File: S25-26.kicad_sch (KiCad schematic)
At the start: 17 parts, among them IC1 CMV4000-3E5M0PN

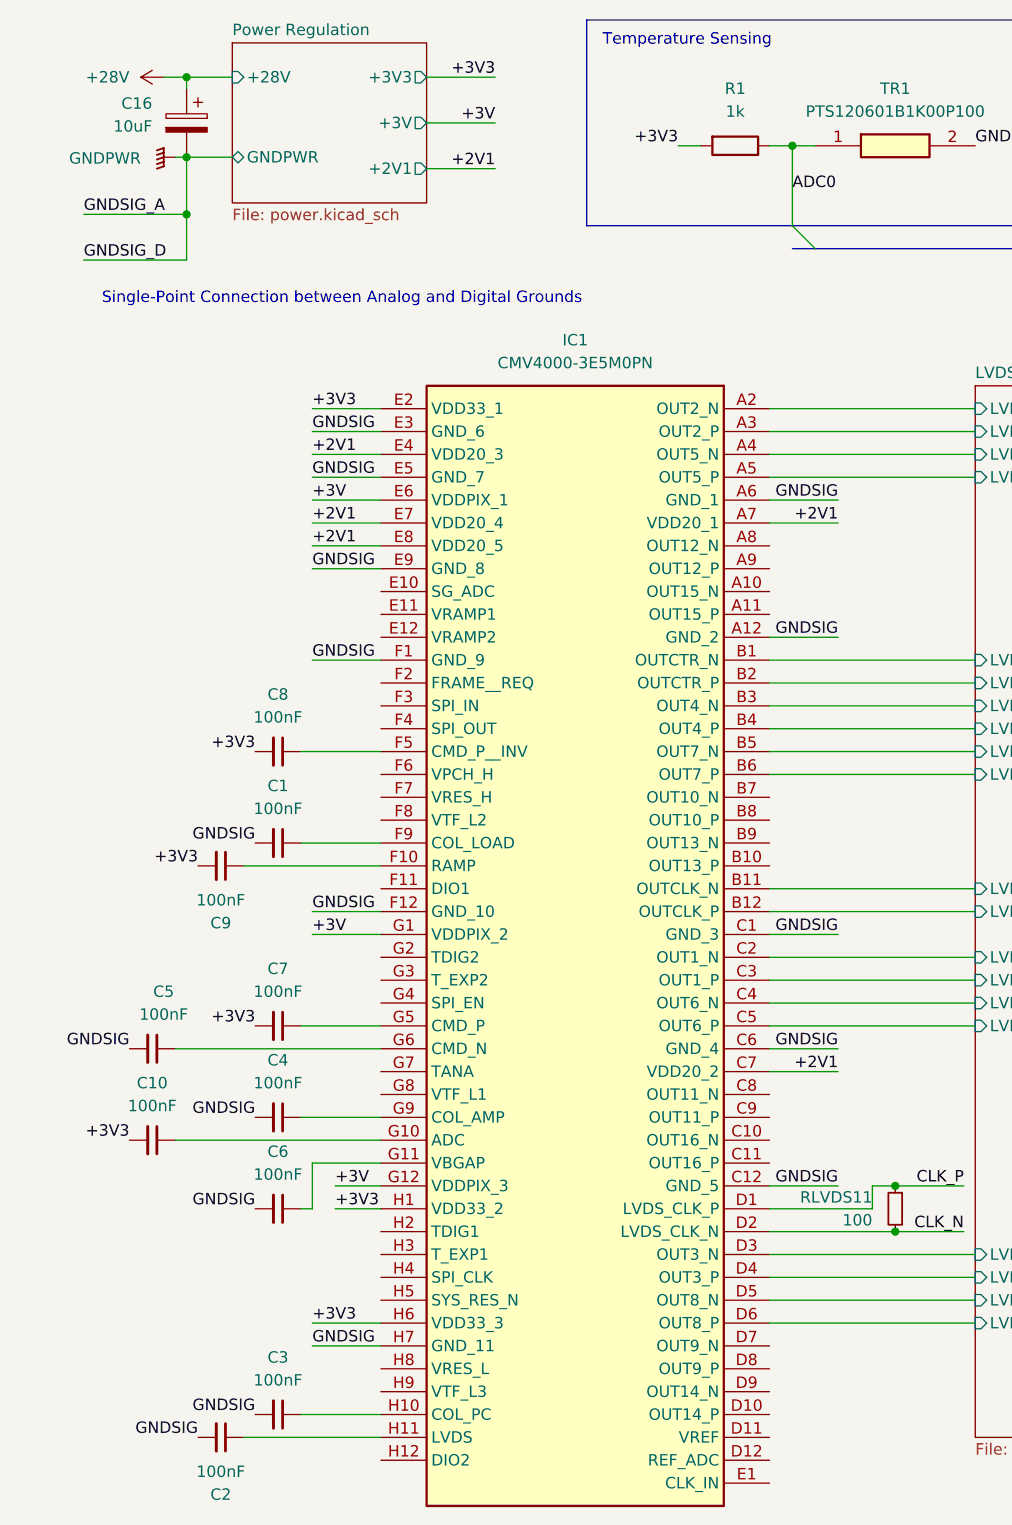
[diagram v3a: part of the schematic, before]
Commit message: Some Colors; GND net ties
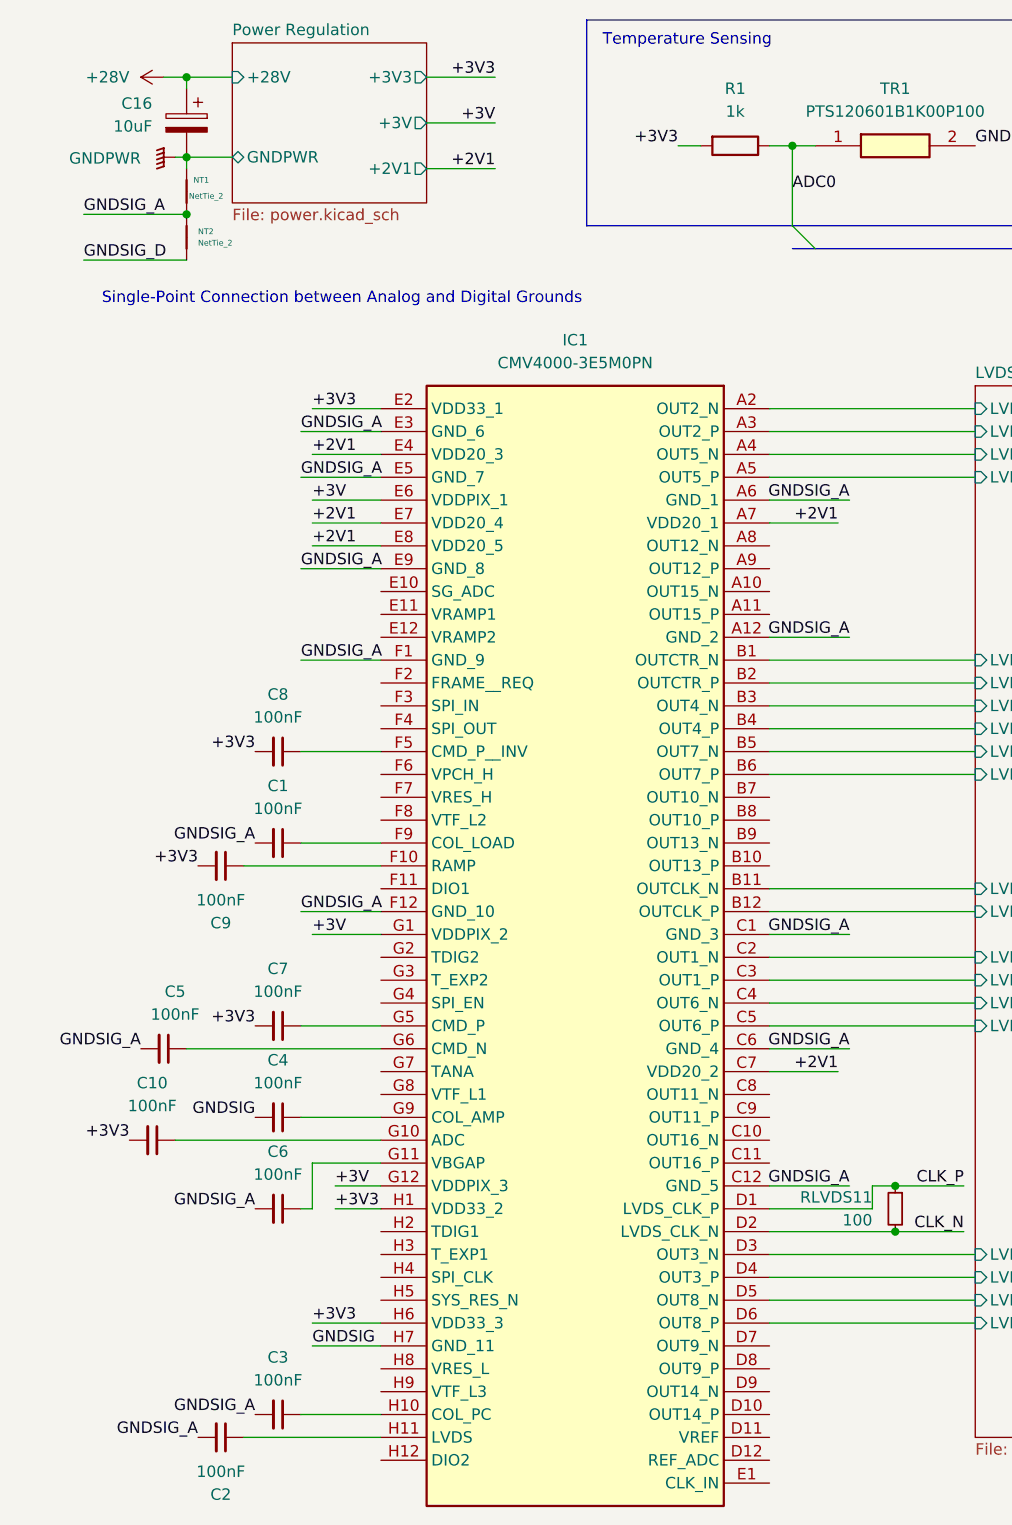
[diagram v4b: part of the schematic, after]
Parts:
- added NT1, NT2: NetTie_2, symbol Device:NetTie_2
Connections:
- net GNDPWR: now also NT1.2
- net GNDSIG: no longer C1.2, C2.2, C3.2, C5.2, C6.2, IC1.A12 (GND_2), IC1.A6 (GND_1), IC1.C1 (GND_3), IC1.C12 (GND_5), IC1.C6 (GND_4), IC1.E3 (GND_6), IC1.E5 (GND_7), IC1.E9 (GND_8), IC1.F1 (GND_9), IC1.F12 (GND_10)
- new net GNDSIG_A: C1.2, C2.2, C3.2, C5.2, C6.2, IC1.A12 (GND_2), IC1.A6 (GND_1), IC1.C1 (GND_3), IC1.C12 (GND_5), IC1.C6 (GND_4), IC1.E3 (GND_6), IC1.E5 (GND_7), IC1.E9 (GND_8), IC1.F1 (GND_9), IC1.F12 (GND_10), NT1.1, NT2.2
- new net GNDSIG_D: NT2.1
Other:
- moved on the sheet: C5
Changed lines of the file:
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@@
 	(wire
 		(pts
-			(xy 40.64 85.09) (xy 48.26 85.09)
+			(xy 39.37 85.09) (xy 48.26 85.09)
 		)
 		(stroke
@@
 	(wire
 		(pts
-			(xy 26.67 29.21) (xy 26.67 35.56)
-		)
-		(stroke
-			(width 0)
-			(type default)
-		)
-	)
-	(wire
-		(pts
-			(xy 99.06 128.27) (xy 91.44 128.27)
+			(xy 100.33 128.27) (xy 91.44 128.27)
 		)
 		(stroke
@@
 	(wire
 		(pts
-			(xy 26.67 35.56) (xy 26.67 40.64)
-		)
-		(stroke
-			(width 0)
-			(type default)
-		)
-	)
-	(wire
-		(pts
 			(xy 171.45 57.15) (xy 177.8 57.15)
 		)
@@
 	(wire
 		(pts
-			(xy 91.44 143.51) (xy 99.06 143.51)
+			(xy 91.44 143.51) (xy 100.33 143.51)
 		)
 		(stroke
@@
 	(wire
 		(pts
-			(xy 40.64 113.03) (xy 48.26 113.03)
+			(xy 39.37 113.03) (xy 48.26 113.03)
 		)
 		(stroke
@@
 	(wire
 		(pts
+			(xy 26.67 29.21) (xy 26.67 30.48)
+		)
+		(stroke
+			(width 0)
+			(type default)
+		)
+	)
+	(wire
+		(pts
 			(xy 40.64 72.39) (xy 48.26 72.39)
 		)
@@
 	(wire
 		(pts
-			(xy 99.06 82.55) (xy 91.44 82.55)
+			(xy 100.33 82.55) (xy 91.44 82.55)
 		)
 		(stroke
@@
 	(wire
 		(pts
-			(xy 40.64 64.77) (xy 48.26 64.77)
+			(xy 39.37 64.77) (xy 48.26 64.77)
 		)
 		(stroke
@@
 	(wire
 		(pts
-			(xy 25.4 128.27) (xy 48.26 128.27)
+			(xy 26.67 128.27) (xy 48.26 128.27)
 		)
 		(stroke
@@
 	(wire
 		(pts
-			(xy 99.06 67.31) (xy 91.44 67.31)
+			(xy 100.33 67.31) (xy 91.44 67.31)
 		)
 		(stroke
@@
 	(wire
 		(pts
-			(xy 40.64 74.93) (xy 48.26 74.93)
+			(xy 39.37 74.93) (xy 48.26 74.93)
 		)
 		(stroke
@@
 	(wire
 		(pts
-			(xy 99.06 115.57) (xy 91.44 115.57)
+			(xy 100.33 115.57) (xy 91.44 115.57)
 		)
 		(stroke
@@
 	(wire
 		(pts
-			(xy 40.64 59.69) (xy 48.26 59.69)
+			(xy 39.37 59.69) (xy 48.26 59.69)
 		)
 		(stroke
@@
 		)
 	)
-	(label "GNDSIG"
-		(at 99.06 115.57 180)
+	(label "GNDSIG_A"
+		(at 100.33 115.57 180)
 		(fields_autoplaced yes)
 		(effects
@@
 		)
 	)
-	(label "GNDSIG"
+	(label "GNDSIG_A"
 		(at 34.29 105.41 180)
 		(fields_autoplaced yes)
@@
 	(label "ADC0"
 		(at 171.45 57.15 0)
+		(fields_autoplaced yes)
 		(effects
 			(font
@@
 		)
 	)
-	(label "GNDSIG"
-		(at 99.06 67.31 180)
+	(label "GNDSIG_A"
+		(at 100.33 67.31 180)
 		(fields_autoplaced yes)
 		(effects
@@
 		)
 	)
-	(label "GNDSIG"
+	(label "GNDSIG_A"
 		(at 34.29 146.05 180)
 		(fields_autoplaced yes)
@@
 		)
 	)
-	(label "GNDSIG"
+	(label "GNDSIG_A"
 		(at 34.29 168.91 180)
 		(fields_autoplaced yes)
@@
 	(label "ADC1"
 		(at 142.24 33.02 0)
+		(fields_autoplaced yes)
 		(effects
 			(font
@@
 		)
 	)
-	(label "GNDSIG"
-		(at 40.64 85.09 0)
+	(label "GNDSIG_A"
+		(at 39.37 85.09 0)
 		(fields_autoplaced yes)
 		(effects
@@
 		)
 	)
-	(label "GNDSIG"
-		(at 40.64 74.93 0)
+	(label "GNDSIG_A"
+		(at 39.37 74.93 0)
 		(fields_autoplaced yes)
 		(effects
@@
 	(label "ADC1"
 		(at 171.45 60.96 0)
+		(fields_autoplaced yes)
 		(effects
 			(font
@@
 		)
 	)
-	(label "GNDSIG"
-		(at 20.32 128.27 180)
+	(label "GNDSIG_A"
+		(at 21.59 128.27 180)
 		(fields_autoplaced yes)
 		(effects
@@
 		)
 	)
-	(label "GNDSIG"
-		(at 40.64 64.77 0)
+	(label "GNDSIG_A"
+		(at 39.37 64.77 0)
 		(fields_autoplaced yes)
 		(effects
@@
 	(label "ADC0"
 		(at 93.98 33.02 0)
+		(fields_autoplaced yes)
 		(effects
 			(font
@@
 		)
 	)
-	(label "GNDSIG"
-		(at 99.06 82.55 180)
+	(label "GNDSIG_A"
+		(at 100.33 82.55 180)
 		(fields_autoplaced yes)
 		(effects
@@
 		)
 	)
-	(label "GNDSIG"
-		(at 99.06 143.51 180)
+	(label "GNDSIG_A"
+		(at 100.33 143.51 180)
 		(fields_autoplaced yes)
 		(effects
@@
 		)
 	)
-	(label "GNDSIG"
-		(at 99.06 128.27 180)
+	(label "GNDSIG_A"
+		(at 100.33 128.27 180)
 		(fields_autoplaced yes)
 		(effects
@@
 		)
 	)
-	(label "GNDSIG"
+	(label "GNDSIG_A"
 		(at 27.94 171.45 180)
 		(fields_autoplaced yes)
@@
 		)
 	)
-	(label "GNDSIG"
-		(at 40.64 59.69 0)
+	(label "GNDSIG_A"
+		(at 39.37 59.69 0)
 		(fields_autoplaced yes)
 		(effects
@@
 		)
 	)
-	(label "GNDSIG"
-		(at 40.64 113.03 0)
+	(label "GNDSIG_A"
+		(at 39.37 113.03 0)
 		(fields_autoplaced yes)
 		(effects
@@
 	)
 	(symbol
+		(lib_id "Device:NetTie_2")
+		(at 26.67 33.02 90)
+		(unit 1)
+		(exclude_from_sim no)
+		(in_bom no)
+		(on_board yes)
+		(dnp no)
+		(property "Reference" "NT1"
+			(at 27.432 31.75 90)
+			(effects
+				(font
+					(size 0.635 0.635)
+				)
+				(justify right)
+			)
+		)
+		(property "Value" "NetTie_2"
+			(at 26.924 33.528 90)
+			(effects
+				(font
+					(size 0.635 0.635)
+				)
+				(justify right)
+			)
+		)
+		(property "Footprint" ""
+			(at 26.67 33.02 0)
+			(effects
+				(font
+					(size 1.27 1.27)
+				)
+				(hide yes)
+			)
+		)
+		(property "Datasheet" "~"
+			(at 26.67 33.02 0)
+			(effects
+				(font
+					(size 1.27 1.27)
+				)
+				(hide yes)
+			)
+		)
+		(property "Description" "Net tie, 2 pins"
+			(at 26.67 33.02 0)
+			(effects
+				(font
+					(size 1.27 1.27)
+				)
+				(hide yes)
+			)
+		)
+		(pin "1"
+		)
+		(pin "2"
+		)
+		(instances
+			(project ""
+				(path "/6f4563ef-8a79-4567-b913-33c6dfb42b56"
+					(reference "NT1")
+					(unit 1)
+				)
+			)
+		)
+	)
+	(symbol
 		(lib_id "Device:R")
 		(at 135.89 27.94 270)
@@
 	)
 	(symbol
+		(lib_id "Device:NetTie_2")
+		(at 26.67 38.1 90)
+		(unit 1)
+		(exclude_from_sim no)
+		(in_bom no)
+		(on_board yes)
+		(dnp no)
+		(fields_autoplaced yes)
+		(property "Reference" "NT2"
+			(at 27.94 37.465 90)
+			(effects
+				(font
+					(size 0.635 0.635)
+				)
+				(justify right)
+			)
+		)
+		(property "Value" "NetTie_2"
+			(at 27.94 38.735 90)
+			(effects
+				(font
+					(size 0.635 0.635)
+				)
+				(justify right)
+			)
+		)
+		(property "Footprint" ""
+			(at 26.67 38.1 0)
+			(effects
+				(font
+					(size 1.27 1.27)
+				)
+				(hide yes)
+			)
+		)
+		(property "Datasheet" "~"
+			(at 26.67 38.1 0)
+			(effects
+				(font
+					(size 1.27 1.27)
+				)
+				(hide yes)
+			)
+		)
+		(property "Description" "Net tie, 2 pins"
+			(at 26.67 38.1 0)
+			(effects
+				(font
+					(size 1.27 1.27)
+				)
+				(hide yes)
+			)
+		)
+		(pin "1"
+		)
+		(pin "2"
+		)
+		(instances
+			(project "S25-26"
+				(path "/6f4563ef-8a79-4567-b913-33c6dfb42b56"
+					(reference "NT2")
+					(unit 1)
+				)
+			)
+		)
+	)
+	(symbol
 		(lib_id "Device:C_Small")
 		(at 30.48 171.45 270)
@@
 	(symbol
 		(lib_id "Device:C_Small")
-		(at 22.86 128.27 270)
+		(at 24.13 128.27 270)
 		(unit 1)
 		(exclude_from_sim no)
@@
 		(dnp no)
 		(property "Reference" "C5"
-			(at 24.1236 121.92 90)
+			(at 25.3936 121.92 90)
 			(effects
 				(font
@@
 		)
 		(property "Value" "100nF"
-			(at 24.1236 124.46 90)
+			(at 25.3936 124.46 90)
 			(effects
 				(font
@@
 		)
 		(property "Footprint" ""
-			(at 22.86 128.27 0)
+			(at 24.13 128.27 0)
 			(effects
 				(font
@@
 		)
 		(property "Datasheet" "~"
-			(at 22.86 128.27 0)
+			(at 24.13 128.27 0)
 			(effects
 				(font
@@
 		)
 		(property "Description" "Unpolarized capacitor, small symbol"
-			(at 22.86 128.27 0)
+			(at 24.13 128.27 0)
 			(effects
 				(font
@@
 		)
 		(fill
-			(color 0 0 0 0.0000)
+			(color 255 255 194 1.0000)
 		)
 		(property "Sheetname" "Power Regulation"
@@
 		)
 		(fill
-			(color 0 0 0 0.0000)
+			(color 255 255 194 1.0000)
 		)
 		(property "Sheetname" "Processing"
@@
 		)
 		(fill
-			(color 0 0 0 0.0000)
+			(color 255 255 194 1.0000)
 		)
 		(property "Sheetname" "LVDS Serialization"

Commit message: Condensed to one page schematic; added decoupling capacitors on MCU; added CLK connections, currently assuming any PWM pins can act as clkout, docs are rather vague; redid LVDS connections to represent CMOS sensor in 8 channel mode with alternating enabled channels; added design rules from JLCPCB for event layout DRC checks
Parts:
- removed C16: 10uF, symbol Device:C_Polarized
- removed NT1, NT2: NetTie_2, symbol Device:NetTie_2
- added 2v1, 3v0, 3v3, VCORE, XRES: TestPoint, TestPoint:TestPoint_Pad_D1.0mm, symbol Connector:TestPoint
- added C11, C14, C19, C20, C22: 0.1uF, symbol Device:C_Polarized
- added C12, C17, C18, C21: 1nF, symbol Device:C_Polarized
- added C13: 15pF, symbol Device:C
- added C15: 0.1uF, symbol Device:C
- added C16: 10uF, symbol Device:C_Small
- added C23: 0.1F, symbol Device:C
- added C26, C27, C28, C29, C30, C31, C32, C33, C34, C35: 100nF, symbol Device:C_Small
- added C36, CAdj4: 10uF, symbol Device:C_Polarized
- added C37, C38, C39, C40, C41, C42, C44, C45, C46, C48, C49, C51, C52, C53, C54, C56, C59, C62, C64: 0.1uF, symbol Device:C_Small
- added C43, C47, C50, C55, C58: 1uF, symbol Device:C_Small
- added C57, C60: 10nF, symbol Device:C_Small
- added C61, C63: 2.2uF, symbol Device:C_Small
- added C65: 10uF, symbol Device:C
- added CAdj5, CAdj6: 10nF, symbol Device:C_Polarized
- added Cin4, Cin5, Cin6, Co4, Co5, Co6: 1uF, symbol Device:C_Polarized
- added D1, D2: 1N4002, Diode_THT:D_DO-41_SOD81_P10.16mm_Horizontal, symbol Diode:1N4002
- added IC10, IC9: MT29F2G01ABAGDWB-IT_G_TR, SON127P800X600X65-8N, symbol SamacSys_Parts:MT29F2G01ABAGDWB-IT_G_TR
- added IC13: DS90LV011AHMF_NOPB, SOT95P280X145-5N, symbol SamacSys_Parts:DS90LV011AHMF_NOPB
- added IC2: XMC7200D-E272K8384AA, BGA272C80P18X18_1600X1600X170, symbol SamacSys_Parts:XMC7200D-E272K8384AA
- added IC3, IC4, IC5: DS90LV048ATM_NOPB, SOIC127P600X175-16N, symbol SamacSys_Parts:DS90LV048ATM_NOPB
- added IC6: NCV317BD2TR4G, TO254P1420X457-4N, symbol SamacSys_Parts:NCV317BD2TR4G
- added IC7: MXL86110I-AQB-R, QFN40P500X500X95-41N-D, symbol SamacSys_Parts:MXL86110C-AQB-R
- added NT3, NT4: NetTie_2, symbol Device:NetTie_2
- added Q2: ZXT849K, symbol Simulation_SPICE:NPN
- added R4: 0.1, symbol Device:R
- added RLVDS1, RLVDS13, RLVDS2, RLVDS3, RLVDS4, RLVDS5, RLVDS6, RLVDS7, RLVDS8, RLVDS9: 100, symbol Device:R_Small
- added RP1_3: 164, symbol Device:R
- added RP1_4, RP2_3: 100, symbol Device:R
- added RP2_4: 150, symbol Device:R
- added RP3_3: 120, symbol Device:R
- added RP3_4: 90, symbol Device:R
- added U1, U2: TPS73601DBV, Package_TO_SOT_SMD:SOT-23-5, symbol Regulator_Linear:TPS73601DBV
- added Y1: DSC1101DM2-012.0000, DSC1101DM20120000, symbol SamacSys_Parts:DSC1101DM2-012.0000
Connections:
- net GNDSIG is gone; now on net GNDSIG_A: C4.2, IC1.H7 (GND_11), TR1.2, TR2.2
- net +2V1: now also 2v1.1, CAdj6.1, Co5.1, RP3_3.1, U2.5 (OUT)
- net +3V: now also 3v0.1, CAdj5.1, Co6.1, RP2_3.1, U1.5 (OUT)
- net +3V3: now also 3v3.1, C11.1, C12.1, C14.1, C15.1, C16.1, C17.1, C18.1, C19.1, C20.1, C21.1, C22.1, C23.1, C37.1, C38.1, C39.1, C40.1, C41.1, C42.1, C43.1, C44.1, C45.1, C46.1, C47.1, C48.1, C49.1, C55.1, C56.1, C57.1, C58.1, C59.1, C60.1, C61.1, C62.1, C63.1, C64.1, Cin5.1, Cin6.1, Co4.1, D1.2 (A), D2.1 (K), IC10.8 (VCC), IC13.1 (VDD), IC2.F10 (VDDIO__1_2), IC2.F11 (VDDIO_1), IC2.F8 (VDDD_1), IC2.F9 (VDDIO__1_1), IC2.H13 (VDDD_2), IC2.H6 (VDDIO_3_1), IC2.J13 (VDDD_3), IC2.J6 (VDDIO_3_2), IC2.K13 (VDDD_4), IC2.K6 (VREFH), IC2.L13 (VDDD_5), IC2.L6 (VDDA), IC2.N10 (VDDIO_4), IC2.N11 (VDDD_6), IC2.N8 (VDDIO__2), IC2.N9 (VDDIO__4), IC3.13 (VCC), IC4.13 (VCC), IC5.13 (VCC), IC6.4 (VOUT_TAB), IC7.11 (VDDA3V3_1), IC7.29 (VDD3V3), IC7.40 (VDDA3V3_2), IC9.8 (VCC), Q2.1 (C), RP1_4.1, U1.1 (IN), U1.3 (EN), U2.1 (IN), U2.3 (EN), Y1.6 (VDD)
- net GNDPWR: now also C36.2, CAdj4.2, Cin4.2, Cin5.2, Cin6.2, Co4.2, Co5.2, Co6.2, NT3.2, NT4.2, RP1_3.2, RP2_4.2, RP3_4.2, U1.2 (GND), U2.2 (GND)
- net GNDSIG_A: now also IC1.G8 (VTF_L1), C11.2, C12.2, C17.2, C18.2, C19.2, C20.2, C21.2, C22.2, C26.2, C27.2, C28.2, C29.2, C30.2, C31.2, C32.2, C33.2, C34.2, C35.2, C61.2, C62.2, C63.2, C64.2, IC13.2 (GND), IC2.K8 (VREFL), IC2.L8 (VSSA), IC3.12 (GND), IC4.12 (GND), IC5.12 (GND), NT3.1
- net GNDSIG_D: now also C13.2, C14.2, C16.2, C37.2, C38.2, C39.2, C40.2, C41.2, C42.2, C43.2, C44.2, C45.2, C46.2, C47.2, C48.2, C49.2, C50.2, C51.2, C52.2, C53.2, C54.2, C55.2, C56.2, C57.2, C58.2, C59.2, C60.2, C65.2, IC2.A1 (VSSD_1), IC2.A18 (VSSD_2), IC2.D9 (VSSD_3), IC2.G12 (VSSD_5), IC2.G7 (VSSD_4), IC2.H10 (VSSD_7), IC2.H11 (VSSD_8), IC2.H8 (VSSIO__3_1), IC2.H9 (VSSD_6), IC2.J10 (VSSD_10), IC2.J11 (VSSD_11), IC2.J15 (VSSD_12), IC2.J8 (VSSIO__3_2), IC2.J9 (VSSD_9), IC2.K10 (VSSD_14), IC2.K11 (VSSD_15), IC2.K9 (VSSD_13), IC2.L10 (VSSIO__4_2), IC2.L11 (VSSD__1), IC2.L18 (VSSD__2_1), IC2.L9 (VSSIO__4_1), IC2.M12 (VSSD_17), IC2.M7 (VSSD_16), IC2.P18 (VSSD__2_2), IC2.R14 (VSSD_19), IC2.R5 (VSSD_18), IC2.V1 (VSSD_20), IC2.V18 (VSSD_21), NT4.1, Y1.3 (GND)
- net CMOS_CH15_N: now reaches IC1.A10 (OUT15_N)
- net CMOS_CH15_N: now also IC4.8 (RIN4-), RLVDS8.1
- net CMOS_CH15_P: now reaches IC1.A11 (OUT15_P)
- net CMOS_CH15_P: now also IC4.7 (RIN4+), RLVDS8.2
- net CMOS_CH13_P: now reaches IC1.B10 (OUT13_P)
- net CMOS_CH13_P: now also IC4.6 (RIN3+), RLVDS7.1
- net CMOS_CH13_N: now reaches IC1.B9 (OUT13_N)
- net CMOS_CH13_N: now also IC4.5 (RIN3-), RLVDS7.2
- net CMOS_CH11_N: now reaches IC1.C8 (OUT11_N)
- net CMOS_CH11_N: now also IC4.4 (RIN2-), RLVDS6.2
- net CMOS_CH11_P: now reaches IC1.C9 (OUT11_P)
- net CMOS_CH11_P: now also IC4.3 (RIN2+), RLVDS6.1
- net at IC1.D11 (VREF): now also C32.1
- net at IC1.D12 (REF_ADC): now also C33.1
- net CMOS_CH09_N: now reaches IC1.D7 (OUT9_N)
- net CMOS_CH09_N: now also IC4.1 (RIN1-), RLVDS5.1
- net CMOS_CH09_P: now reaches IC1.D8 (OUT9_P)
- net CMOS_CH09_P: now also IC4.2 (RIN1+), RLVDS5.2
- net CMOS_LVDS_CLK_IN: now reaches IC1.E1 (CLK_IN)
- net CMOS_LVDS_CLK_IN: now also IC13.5 (TTL_IN), IC2.E1 (P7.0), IC2.F1 (P7.2)
- net at IC1.E10 (SG_ADC): now also C26.1
- net at IC1.E11 (VRAMP1): now also C27.1
- net at IC1.E12 (VRAMP2): now also C28.1
- net FRAME_REQ: now reaches IC1.F2 (FRAME__REQ)
- net CMOS_SPI_MOSI: now reaches IC1.F3 (SPI_IN)
- net CMOS_SPI_MOSI: now also IC2.G15 (P23.1)
- net CMOS_SPI_MISO: now reaches IC1.F4 (SPI_OUT)
- net CMOS_SPI_MISO: now also IC2.G16 (P23.0)
- net at IC1.F6 (VPCH_H): now also C29.1
- net at IC1.F7 (VRES_H): now also C30.1
- net at IC1.F8 (VTF_L2): now also C31.1
- net CMOS_SPI_EN: now reaches IC1.G4 (SPI_EN)
- net CMOS_SPI_EN: now also IC2.F2 (P7.3)
- net CMOS_SPI_CLK: now reaches IC1.H4 (SPI_CLK)
- net CMOS_SPI_CLK: now also IC2.G13 (P23.2)
- net CMOS_RESET_N: now reaches IC1.H5 (SYS_RES_N)
- net at IC1.H8 (VRES_L): now also C35.1
- net at IC1.H9 (VTF_L3): now also C34.1
- net ADC0 renamed TEMPR_ADC0
- net TEMPR_ADC0: now also IC2.B4 (P6.0)
- net ADC1 renamed TEMPR_ADC1
- net TEMPR_ADC1: now also IC2.C4 (P6.1)
- net CLK_N renamed CMOS_CLK_IN_N
- net CMOS_CLK_IN_N: now also IC13.3 (OUT-), IC13.4 (OUT+)
- net CLK_P renamed CMOS_CLK_IN_P
- net LVDS Serialization/LVDS_1N renamed CMOS_CH01_N
- net CMOS_CH01_N: now also IC3.1 (RIN1-), RLVDS1.1
- net LVDS Serialization/LVDS_1P renamed CMOS_CH01_P
- net CMOS_CH01_P: now also IC3.2 (RIN1+), RLVDS1.2
- net LVDS Serialization/LVDS_2N: no longer names the net of IC1.A2 (OUT2_N)
- net LVDS Serialization/LVDS_2P: no longer names the net of IC1.A3 (OUT2_P)
- net LVDS Serialization/LVDS_3N renamed CMOS_CH03_N
- net CMOS_CH03_N: now also IC3.4 (RIN2-), RLVDS2.2
- net LVDS Serialization/LVDS_3P renamed CMOS_CH03_P
- net CMOS_CH03_P: now also IC3.3 (RIN2+), RLVDS2.1
- net LVDS Serialization/LVDS_4N: no longer names the net of IC1.B3 (OUT4_N)
- net LVDS Serialization/LVDS_4P: no longer names the net of IC1.B4 (OUT4_P)
- net LVDS Serialization/LVDS_5N renamed CMOS_CH05_N
- net CMOS_CH05_N: now also IC3.5 (RIN3-), RLVDS3.2
- net LVDS Serialization/LVDS_5P renamed CMOS_CH05_P
- net CMOS_CH05_P: now also IC3.6 (RIN3+), RLVDS3.1
- net LVDS Serialization/LVDS_6N: no longer names the net of IC1.C4 (OUT6_N)
- net LVDS Serialization/LVDS_6P: no longer names the net of IC1.C5 (OUT6_P)
- net LVDS Serialization/LVDS_7N renamed CMOS_CH07_N
- net CMOS_CH07_N: now also IC3.8 (RIN4-), RLVDS4.1
- net LVDS Serialization/LVDS_7P renamed CMOS_CH07_P
- net CMOS_CH07_P: now also IC3.7 (RIN4+), RLVDS4.2
- net LVDS Serialization/LVDS_8N: no longer names the net of IC1.D5 (OUT8_N)
- net LVDS Serialization/LVDS_8P: no longer names the net of IC1.D6 (OUT8_P)
- net LVDS Serialization/LVDS_CLKN renamed CMOS_CLK_OUT_N
- net CMOS_CLK_OUT_N: now also IC5.1 (RIN1-), RLVDS9.1
- net LVDS Serialization/LVDS_CLKP renamed CMOS_CLK_OUT_P
- net CMOS_CLK_OUT_P: now also IC5.2 (RIN1+), RLVDS9.2
- net LVDS Serialization/LVDS_CTRN renamed CMOS_CTR_OUT_N
- net CMOS_CTR_OUT_N: now also IC5.8 (RIN4-), RLVDS13.1
- net LVDS Serialization/LVDS_CTRP renamed CMOS_CTR_OUT_P
- net CMOS_CTR_OUT_P: now also IC5.7 (RIN4+), RLVDS13.2
- new net: CAdj6.2, RP3_3.2, RP3_4.1, U2.4 (FB)
- new net: CAdj4.1, D2.2 (A), IC6.1 (ADJ), RP1_3.1, RP1_4.2
- new net: CAdj5.2, RP2_3.2, RP2_4.1, U1.4 (FB)
- new net: IC2.K18 (XRES__L), XRES.1
- new net CMOS_CH01: IC2.A6 (P5.0), IC3.15 (ROUT1)
- new net CMOS_CH03: IC2.A8 (P4.0), IC3.14 (ROUT2)
- new net CMOS_CH05: IC2.C6 (P5.2), IC3.11 (ROUT3)
- new net CMOS_CH07: IC3.10 (ROUT4)
- new net CMOS_CH09: IC4.15 (ROUT1)
- new net CMOS_CH11: IC4.14 (ROUT2)
- new net CMOS_CH13: IC2.D8 (P4.3), IC4.11 (ROUT3)
- new net CMOS_CH15: IC2.D6 (P5.3), IC4.10 (ROUT4)
- new net CMOS_CLK_OUT: IC5.10 (ROUT4)
- new net CMOS_CTR: IC2.D17 (P28.3), IC5.15 (ROUT1)
- new net DC_LINE_IN: C36.1, Cin4.1, D1.1 (K), IC6.3 (VIN)
- new net DRV_VOUT: Q2.2 (B)
- new net ECO_IN: C13.1, IC2.M18 (P21.3), Y1.4 (OUT)
- new net ETH0_ETH_TSU_TIMER_CMP_VAL: IC2.D14 (P2.3)
- new net ETH0_MDC: IC2.A12 (P3.1), IC7.13 (MDC)
- new net ETH0_MDIO: IC2.A13 (P3.0), IC7.14 (MDIO)
- new net ETH0_REF_CLK: IC2.U18 (P18.0)
- new net ETH0_RXD_0: IC2.R18 (P19.0), IC7.18 (TXD0)
- new net ETH0_RXD_1: IC2.R17 (P19.1), IC7.17 (TXD1)
- new net ETH0_RXD_2: IC2.P17 (P19.2), IC7.16 (TXD2)
- new net ETH0_RXD_3: IC2.P16 (P19.3), IC7.15 (TXD3)
- new net ETH0_RX_CLK: IC2.F17 (P23.3), IC7.20 (TX_CLK)
- new net ETH0_RX_CTL: IC2.K17 (P21.5), IC7.19 (TX_CTL)
- new net ETH0_RX_ER: IC2.C14 (P2.2)
- new net ETH0_TXD_0: IC2.T16 (P18.4), IC7.25 (RXD0/RXDLY)
- new net ETH0_TXD_1: IC2.R16 (P18.5), IC7.24 (RXD1/TXDLY)
- new net ETH0_TXD_2: IC2.R15 (P18.6), IC7.23 (RXD2/PLLOFF)
- new net ETH0_TXD_3: IC2.P15 (P18.7), IC7.22 (RXD3/PHYAD0)
- new net ETH0_TX_CLK: IC2.T17 (P18.3), IC7.27 (RX_CLK/PHYAD1)
- new net ETH0_TX_CTL: IC2.U17 (P18.1), IC7.26 (RX_CTL/PHYAD2)
- new net ETH0_TX_ER: IC2.T18 (P18.2)
- new net EXT_PS_CTL0: IC2.H18 (P22.1), Q2.3 (E), R4.1
- new net EXT_PS_CTL1: C50.1, C51.1, C52.1, C53.1, C54.1, C65.1, IC2.F13 (VCCD_2), IC2.F6 (VCCD_1), IC2.G18 (P22.2), IC2.N13 (VCCD_4), IC2.N6 (VCCD_3), R4.2, VCORE.1
- new net GND: C15.2, C23.2, IC10.4 (VSS), IC7.41 (EP), IC9.4 (VSS)
- new net JTAG_SWCLK: IC2.F15 (P23.5)
- new net JTAG_SWDIO: IC2.E18 (P23.6)
- new net JTAG_SWO: IC2.F16 (P23.4)
- new net JTAG_TDI: IC2.E17 (P23.7)
- new net LVDS_RECV_EN: IC3.16 (EN), IC4.16 (EN), IC5.16 (EN)
- new net SCB0_CLK: IC2.A17 (P0.2), IC9.6 (SCK)
- new net SCB0_MISO: IC2.B18 (P0.0), IC9.2 (SO/IO1)
- new net SCB0_MOSI: IC2.B17 (P0.1), IC9.5 (SI/IO0)
- new net SCB0_SEL0: IC2.B16 (P0.3), IC9.1 (CS#)
- new net SCB2_CLK: IC10.6 (SCK), IC2.U6 (P14.2)
- new net SCB2_MISO: IC10.2 (SO/IO1), IC2.V5 (P14.0)
- new net SCB2_MOSI: IC10.5 (SI/IO0), IC2.V6 (P14.1)
- new net SCB2_SEL0: IC10.1 (CS#), IC2.T6 (P14.3)
- new net SCB3_RX: IC2.U14 (P17.1)
- new net SCB3_TX: IC2.V15 (P17.2)
- new net VDD1V1: IC7.21 (VDD), IC7.3 (VDDA1V1_1), IC7.30 (DCDC_REGO), IC7.38 (VDDA1V1_3), IC7.8 (VDDA1V1_2)
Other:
- removed sheet LVDS Serialization
- removed sheet Power Regulation
- removed sheet Processing
- note added: "CMOS to LVDS Conversion"
- note added: "Core External Regulator"
- note added: "Ethernet PHY Transceiver"
- note added: "External Memory"
- note added: "LVDS to CMOS Conversion"
- note added: "NC"
- note added: "Primary Microcontroller, Infineon XMC7200D"
- note added: "Reference Oscillator"
- note added: "Voltage Regulation"
- note added: "XMC7200D Supply Decoupling Capacitors"
- note added: "ams CMV4000 CMOS Image Sensor"
- company: (none) -> Virginia Tech ECE Major Design Experience
- title: (none) -> S25-26: CMOS Detector Small Satellite Readout System
- moved on the sheet: C1, C10, C2, C3, C4, C5, C6, C7, C8, C9, IC1, R1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
